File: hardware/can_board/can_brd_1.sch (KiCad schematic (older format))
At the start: 9 parts, among them P1 CONN_4, P2 CONN_2, U1 MCP2551

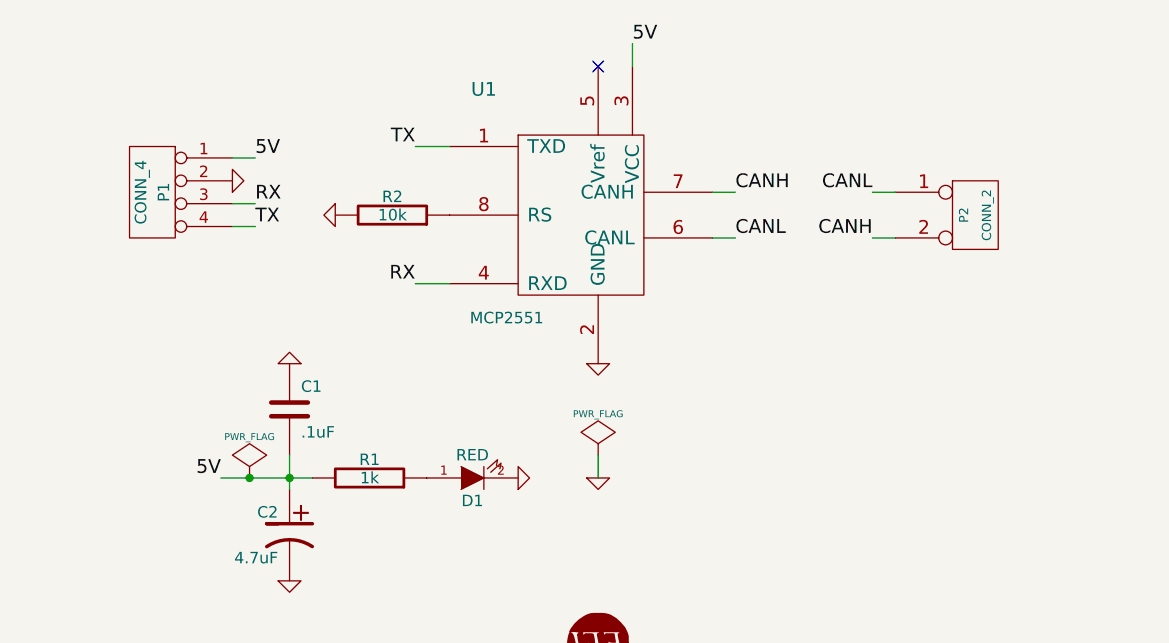
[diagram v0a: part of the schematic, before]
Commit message: 
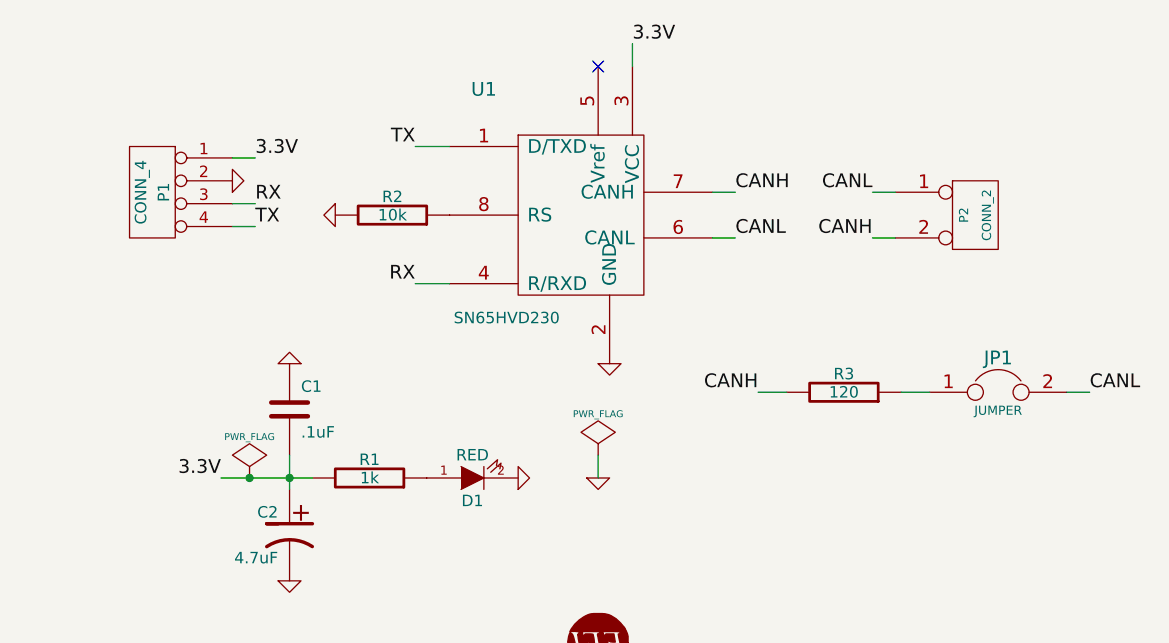
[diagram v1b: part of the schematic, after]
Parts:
- removed U1: MCP2551, symbol MCP2551
- added JP1: JUMPER, symbol JUMPER
- added R3: 120, symbol R
- added U1: SN65HVD230, symbol SN65HVD230
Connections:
- net CANH: now also R3.2, U1.7 (CANH)
- net CANL: now also JP1.2, U1.6 (CANL)
- net GND: now also U1.2 (GND)
- net RX: now also U1.4 (R/RXD)
- net TX: now also U1.1 (D/TXD)
- net at R2.1: now also U1.8 (RS)
- net 5V renamed 3.3V
- net 3.3V: now also U1.3 (VCC)
- new net: JP1.1, R3.1
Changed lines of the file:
@@
 Sheet 1 1
 Title ""
-Date "06 Янв 2014"
+Date "08 Янв 2014"
 Rev ""
 Comp ""
@@
 $EndComp
 Text Label 3250 3000 2    60   ~ 0
-5V
+3.3V
 $Comp
 L LOGO G1
@@
 $EndComp
 $Comp
-L MCP2551 U1
-U 1 1 52CADB33
-P 4800 1850
-F 0 "U1" H 4400 2400 60  0000 C CNN
-F 1 "MCP2551" H 4500 1400 50  0000 C CNN
-F 2 "" H 4800 1850 60  0000 C CNN
-F 3 "" H 4800 1850 60  0000 C CNN
-	1    4800 1850
-	1    0    0    -1
-$EndComp
-$Comp
 L GND #PWR05
 U 1 1 52CADB40
-P 4900 2500
-F 0 "#PWR05" H 4900 2500 30  0001 C CNN
-F 1 "GND" H 4900 2430 30  0001 C CNN
-F 2 "" H 4900 2500 60  0001 C CNN
-F 3 "" H 4900 2500 60  0001 C CNN
-	1    4900 2500
+P 4950 2500
+F 0 "#PWR05" H 4950 2500 30  0001 C CNN
+F 1 "GND" H 4950 2430 30  0001 C CNN
+F 2 "" H 4950 2500 60  0001 C CNN
+F 3 "" H 4950 2500 60  0001 C CNN
+	1    4950 2500
 	1    0    0    -1
 $EndComp
@@
 $EndComp
 Text Label 3400 1600 0    60   ~ 0
-5V
+3.3V
 $Comp
 L GND #PWR07
@@
 	5400 1950 5500 1950
 Text Label 5050 1100 0    60   ~ 0
-5V
+3.3V
 Wire Wire Line
 	5050 1200 5050 1100
@@
 	1    0    0    -1
 $EndComp
+$Comp
+L SN65HVD230 U1
+U 1 1 52CD2CA4
+P 4800 1850
+F 0 "U1" H 4400 2400 60  0000 C CNN
+F 1 "SN65HVD230" H 4500 1400 50  0000 C CNN
+F 2 "" H 4800 1850 60  0000 C CNN
+F 3 "" H 4800 1850 60  0000 C CNN
+	1    4800 1850
+	1    0    0    -1
+$EndComp
+$Comp
+L R R3
+U 1 1 52CD2DE2
+P 5975 2625
+F 0 "R3" V 6055 2625 50  0000 C CNN
+F 1 "120" V 5975 2625 50  0000 C CNN
+F 2 "" H 5975 2625 60  0001 C CNN
+F 3 "" H 5975 2625 60  0001 C CNN
+	1    5975 2625
+	0    1    -1   0
+$EndComp
+$Comp
+L JUMPER JP1
+U 1 1 52CD2DEF
+P 6650 2625
+F 0 "JP1" H 6650 2775 60  0000 C CNN
+F 1 "JUMPER" H 6650 2545 40  0000 C CNN
+F 2 "" H 6650 2625 60  0000 C CNN
+F 3 "" H 6650 2625 60  0000 C CNN
+	1    6650 2625
+	1    0    0    -1
+$EndComp
+Wire Wire Line
+	6225 2625 6350 2625
+Text Label 5600 2625 2    60   ~ 0
+CANH
+Text Label 7050 2625 0    60   ~ 0
+CANL
+Wire Wire Line
+	6950 2625 7050 2625
+Wire Wire Line
+	5725 2625 5600 2625
 $EndSCHEMATC

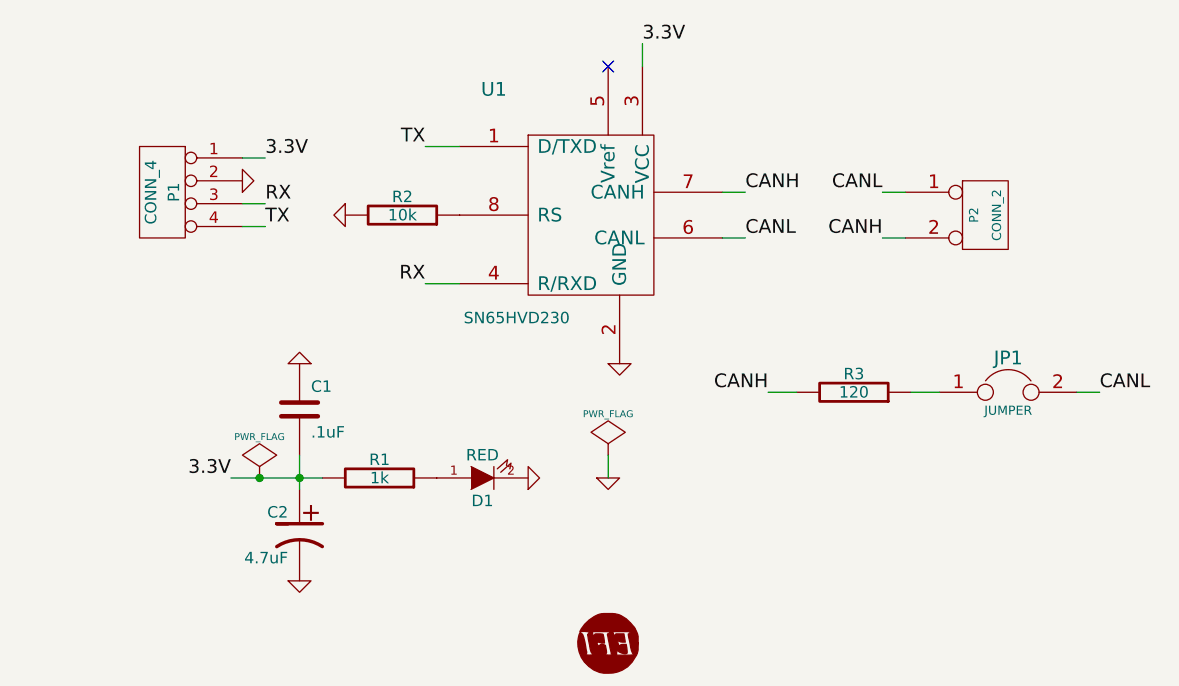
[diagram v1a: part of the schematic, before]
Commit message: 
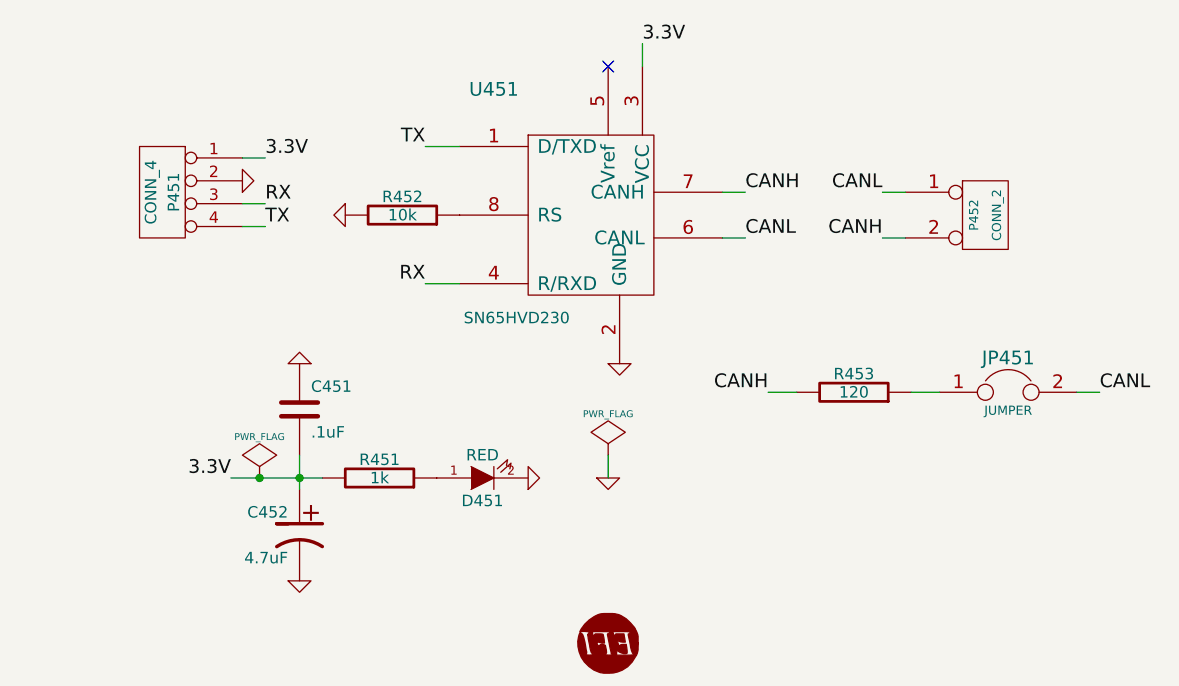
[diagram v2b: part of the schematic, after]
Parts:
- renumbered C1 to C451, C2 to C452, D1 to D451, G1 to G451, JP1 to JP451, P1 to P451, P2 to P452, R1 to R451, R2 to R452, R3 to R453, U1 to U451
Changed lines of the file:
@@
 $EndDescr
 $Comp
-L R R1
+L R R451
 U 1 1 52CAD8DB
 P 3900 3000
-F 0 "R1" V 3980 3000 50  0000 C CNN
+F 0 "R451" V 3980 3000 50  0000 C CNN
 F 1 "1k" V 3900 3000 50  0000 C CNN
 F 2 "" H 3900 3000 60  0001 C CNN
@@
 $EndComp
 $Comp
-L LED D1
+L LED D451
 U 1 1 52CAD8DC
 P 4350 3000
-F 0 "D1" H 4350 3100 50  0000 C CNN
+F 0 "D451" H 4350 3100 50  0000 C CNN
 F 1 "RED" H 4350 2900 50  0000 C CNN
 F 2 "" H 4350 3000 60  0001 C CNN
@@
 $EndComp
 $Comp
-L CP1 C2
+L CP1 C452
 U 1 1 52CAD8F6
 P 3550 3250
-F 0 "C2" H 3600 3350 50  0000 L CNN
+F 0 "C452" H 3600 3350 50  0000 L CNN
 F 1 "4.7uF" H 3600 3150 50  0000 L CNN
 F 2 "" H 3550 3250 60  0001 C CNN
@@
 $EndComp
 $Comp
-L C C1
+L C C451
 U 1 1 52CAD8F7
 P 3550 2700
-F 0 "C1" H 3600 2800 50  0000 L CNN
+F 0 "C451" H 3600 2800 50  0000 L CNN
 F 1 ".1uF" H 3600 2600 50  0000 L CNN
 F 2 "" H 3550 2700 60  0001 C CNN
@@
 3.3V
 $Comp
-L LOGO G1
+L LOGO G451
 U 1 1 52CADA22
 P 4900 3725
-F 0 "G1" H 4900 3622 60  0001 C CNN
+F 0 "G451" H 4900 3622 60  0001 C CNN
 F 1 "LOGO" H 4900 3828 60  0001 C CNN
 F 2 "" H 4900 3725 60  0000 C CNN
@@
 NoConn ~ 4900 1200
 $Comp
-L R R2
+L R R452
 U 1 1 52CADB46
 P 4000 1850
-F 0 "R2" V 4080 1850 50  0000 C CNN
+F 0 "R452" V 4080 1850 50  0000 C CNN
 F 1 "10k" V 4000 1850 50  0000 C CNN
 F 2 "" H 4000 1850 60  0001 C CNN
@@
 $EndComp
 $Comp
-L CONN_2 P2
+L CONN_2 P452
 U 1 1 52CADBC1
 P 6550 1850
-F 0 "P2" V 6500 1850 40  0000 C CNN
+F 0 "P452" V 6500 1850 40  0000 C CNN
 F 1 "CONN_2" V 6600 1850 40  0000 C CNN
 F 2 "" H 6550 1850 60  0000 C CNN
@@
 $EndComp
 $Comp
-L CONN_4 P1
+L CONN_4 P451
 U 1 1 52CADBD0
 P 2950 1750
-F 0 "P1" V 2900 1750 50  0000 C CNN
+F 0 "P451" V 2900 1750 50  0000 C CNN
 F 1 "CONN_4" V 3000 1750 50  0000 C CNN
 F 2 "" H 2950 1750 60  0000 C CNN
@@
 $EndComp
 $Comp
-L SN65HVD230 U1
+L SN65HVD230 U451
 U 1 1 52CD2CA4
 P 4800 1850
-F 0 "U1" H 4400 2400 60  0000 C CNN
+F 0 "U451" H 4400 2400 60  0000 C CNN
 F 1 "SN65HVD230" H 4500 1400 50  0000 C CNN
 F 2 "" H 4800 1850 60  0000 C CNN
@@
 $EndComp
 $Comp
-L R R3
+L R R453
 U 1 1 52CD2DE2
 P 5975 2625
-F 0 "R3" V 6055 2625 50  0000 C CNN
+F 0 "R453" V 6055 2625 50  0000 C CNN
 F 1 "120" V 5975 2625 50  0000 C CNN
 F 2 "" H 5975 2625 60  0001 C CNN
@@
 $EndComp
 $Comp
-L JUMPER JP1
+L JUMPER JP451
 U 1 1 52CD2DEF
 P 6650 2625
-F 0 "JP1" H 6650 2775 60  0000 C CNN
+F 0 "JP451" H 6650 2775 60  0000 C CNN
 F 1 "JUMPER" H 6650 2545 40  0000 C CNN
 F 2 "" H 6650 2625 60  0000 C CNN

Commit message: new location
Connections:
- net RX renamed CAN_RX
- net TX renamed CAN_TX
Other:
- moved on the sheet: P451
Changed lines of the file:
@@
 LIBS:art-electro-ic
 LIBS:logo_flipped
-LIBS:can_brd_1-cache
-EELAYER 24 0
+EELAYER 27 0
 EELAYER END
 $Descr A4 11693 8268
@@
 Sheet 1 1
 Title ""
-Date "08 Янв 2014"
+Date "19 jan 2014"
 Rev ""
 Comp ""
@@
 L CONN_4 P451
 U 1 1 52CADBD0
-P 2950 1750
-F 0 "P451" V 2900 1750 50  0000 C CNN
-F 1 "CONN_4" V 3000 1750 50  0000 C CNN
-F 2 "" H 2950 1750 60  0000 C CNN
-F 3 "" H 2950 1750 60  0000 C CNN
-	1    2950 1750
+P 2200 1750
+F 0 "P451" V 2150 1750 50  0000 C CNN
+F 1 "CONN_4" V 2250 1750 50  0000 C CNN
+F 2 "" H 2200 1750 60  0000 C CNN
+F 3 "" H 2200 1750 60  0000 C CNN
+	1    2200 1750
 	-1   0    0    -1
 $EndComp
-Text Label 3400 1600 0    60   ~ 0
+Text Label 2650 1600 0    60   ~ 0
 3.3V
 $Comp
 L GND #PWR07
 U 1 1 52CADB3B
-P 3300 1700
-F 0 "#PWR07" H 3300 1700 30  0001 C CNN
-F 1 "GND" H 3300 1630 30  0001 C CNN
-F 2 "" H 3300 1700 60  0001 C CNN
-F 3 "" H 3300 1700 60  0001 C CNN
-	1    3300 1700
+P 2550 1700
+F 0 "#PWR07" H 2550 1700 30  0001 C CNN
+F 1 "GND" H 2550 1630 30  0001 C CNN
+F 2 "" H 2550 1700 60  0001 C CNN
+F 3 "" H 2550 1700 60  0001 C CNN
+	1    2550 1700
 	0    -1   -1   0
 $EndComp
-Text Label 3400 1800 0    60   ~ 0
-RX
-Text Label 3400 1900 0    60   ~ 0
-TX
+Text Label 2650 1800 0    60   ~ 0
+CAN_RX
+Text Label 2650 1900 0    60   ~ 0
+CAN_TX
 Text Label 4100 1550 2    60   ~ 0
-TX
+CAN_TX
 Text Label 4100 2150 2    60   ~ 0
-RX
+CAN_RX
 Connection ~ -4675 3450
 Wire Wire Line
@@
 Connection ~ 3375 3000
 Wire Wire Line
-	3300 1800 3400 1800
-Wire Wire Line
-	3300 1900 3400 1900
-Wire Wire Line
-	3300 1600 3400 1600
+	2550 1800 2650 1800
+Wire Wire Line
+	2550 1900 2650 1900
+Wire Wire Line
+	2550 1600 2650 1600
 Wire Wire Line
 	4250 2150 4100 2150

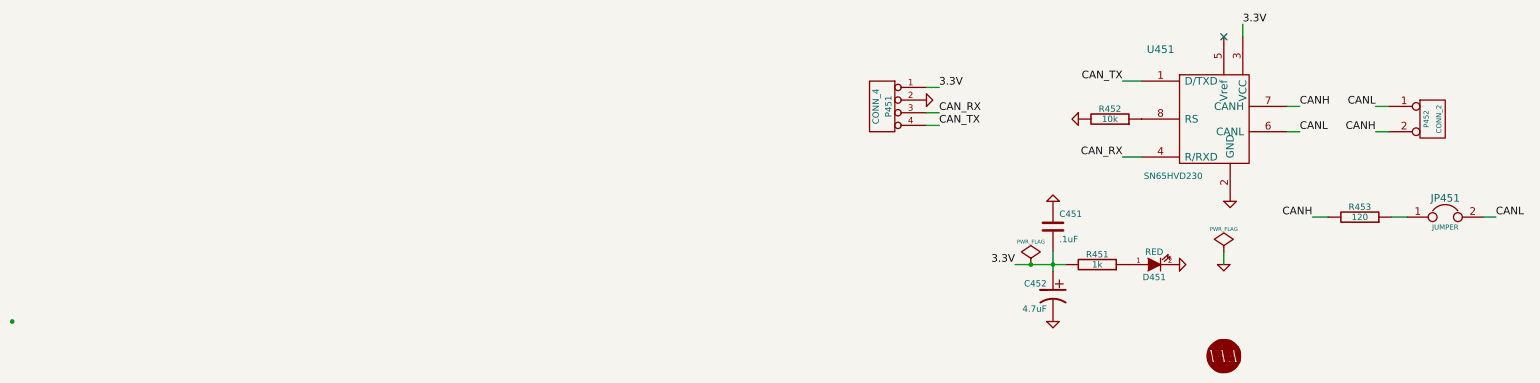
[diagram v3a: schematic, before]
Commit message: name range fix
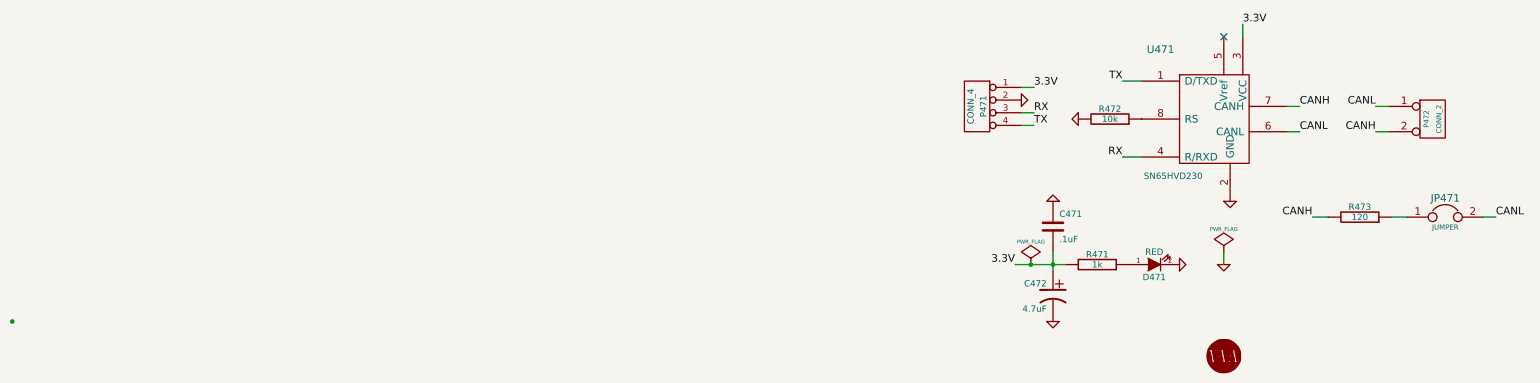
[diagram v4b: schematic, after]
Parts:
- renumbered C451 to C471, C452 to C472, D451 to D471, G451 to G471, JP451 to JP471, P451 to P471, P452 to P472, R451 to R471, R452 to R472, R453 to R473, U451 to U471
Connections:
- net CAN_RX renamed RX
- net CAN_TX renamed TX
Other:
- moved on the sheet: P471
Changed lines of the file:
@@
 LIBS:art-electro-ic
 LIBS:logo_flipped
-EELAYER 27 0
+LIBS:can_brd_1-cache
+EELAYER 24 0
 EELAYER END
 $Descr A4 11693 8268
@@
 Sheet 1 1
 Title ""
-Date "19 jan 2014"
+Date "08 Янв 2014"
 Rev ""
 Comp ""
@@
 $EndDescr
 $Comp
-L R R451
+L R R471
 U 1 1 52CAD8DB
 P 3900 3000
-F 0 "R451" V 3980 3000 50  0000 C CNN
+F 0 "R471" V 3980 3000 50  0000 C CNN
 F 1 "1k" V 3900 3000 50  0000 C CNN
 F 2 "" H 3900 3000 60  0001 C CNN
@@
 $EndComp
 $Comp
-L LED D451
+L LED D471
 U 1 1 52CAD8DC
 P 4350 3000
-F 0 "D451" H 4350 3100 50  0000 C CNN
+F 0 "D471" H 4350 3100 50  0000 C CNN
 F 1 "RED" H 4350 2900 50  0000 C CNN
 F 2 "" H 4350 3000 60  0001 C CNN
@@
 $EndComp
 $Comp
-L CP1 C452
+L CP1 C472
 U 1 1 52CAD8F6
 P 3550 3250
-F 0 "C452" H 3600 3350 50  0000 L CNN
+F 0 "C472" H 3600 3350 50  0000 L CNN
 F 1 "4.7uF" H 3600 3150 50  0000 L CNN
 F 2 "" H 3550 3250 60  0001 C CNN
@@
 $EndComp
 $Comp
-L C C451
+L C C471
 U 1 1 52CAD8F7
 P 3550 2700
-F 0 "C451" H 3600 2800 50  0000 L CNN
+F 0 "C471" H 3600 2800 50  0000 L CNN
 F 1 ".1uF" H 3600 2600 50  0000 L CNN
 F 2 "" H 3550 2700 60  0001 C CNN
@@
 3.3V
 $Comp
-L LOGO G451
+L LOGO G471
 U 1 1 52CADA22
 P 4900 3725
-F 0 "G451" H 4900 3622 60  0001 C CNN
+F 0 "G471" H 4900 3622 60  0001 C CNN
 F 1 "LOGO" H 4900 3828 60  0001 C CNN
 F 2 "" H 4900 3725 60  0000 C CNN
@@
 NoConn ~ 4900 1200
 $Comp
-L R R452
+L R R472
 U 1 1 52CADB46
 P 4000 1850
-F 0 "R452" V 4080 1850 50  0000 C CNN
+F 0 "R472" V 4080 1850 50  0000 C CNN
 F 1 "10k" V 4000 1850 50  0000 C CNN
 F 2 "" H 4000 1850 60  0001 C CNN
@@
 $EndComp
 $Comp
-L CONN_2 P452
+L CONN_2 P472
 U 1 1 52CADBC1
 P 6550 1850
-F 0 "P452" V 6500 1850 40  0000 C CNN
+F 0 "P472" V 6500 1850 40  0000 C CNN
 F 1 "CONN_2" V 6600 1850 40  0000 C CNN
 F 2 "" H 6550 1850 60  0000 C CNN
@@
 $EndComp
 $Comp
-L CONN_4 P451
+L CONN_4 P471
 U 1 1 52CADBD0
-P 2200 1750
-F 0 "P451" V 2150 1750 50  0000 C CNN
-F 1 "CONN_4" V 2250 1750 50  0000 C CNN
-F 2 "" H 2200 1750 60  0000 C CNN
-F 3 "" H 2200 1750 60  0000 C CNN
-	1    2200 1750
+P 2950 1750
+F 0 "P471" V 2900 1750 50  0000 C CNN
+F 1 "CONN_4" V 3000 1750 50  0000 C CNN
+F 2 "" H 2950 1750 60  0000 C CNN
+F 3 "" H 2950 1750 60  0000 C CNN
+	1    2950 1750
 	-1   0    0    -1
 $EndComp
-Text Label 2650 1600 0    60   ~ 0
+Text Label 3400 1600 0    60   ~ 0
 3.3V
 $Comp
 L GND #PWR07
 U 1 1 52CADB3B
-P 2550 1700
-F 0 "#PWR07" H 2550 1700 30  0001 C CNN
-F 1 "GND" H 2550 1630 30  0001 C CNN
-F 2 "" H 2550 1700 60  0001 C CNN
-F 3 "" H 2550 1700 60  0001 C CNN
-	1    2550 1700
+P 3300 1700
+F 0 "#PWR07" H 3300 1700 30  0001 C CNN
+F 1 "GND" H 3300 1630 30  0001 C CNN
+F 2 "" H 3300 1700 60  0001 C CNN
+F 3 "" H 3300 1700 60  0001 C CNN
+	1    3300 1700
 	0    -1   -1   0
 $EndComp
-Text Label 2650 1800 0    60   ~ 0
-CAN_RX
-Text Label 2650 1900 0    60   ~ 0
-CAN_TX
+Text Label 3400 1800 0    60   ~ 0
+RX
+Text Label 3400 1900 0    60   ~ 0
+TX
 Text Label 4100 1550 2    60   ~ 0
-CAN_TX
+TX
 Text Label 4100 2150 2    60   ~ 0
-CAN_RX
+RX
 Connection ~ -4675 3450
 Wire Wire Line
@@
 Connection ~ 3375 3000
 Wire Wire Line
-	2550 1800 2650 1800
-Wire Wire Line
-	2550 1900 2650 1900
-Wire Wire Line
-	2550 1600 2650 1600
+	3300 1800 3400 1800
+Wire Wire Line
+	3300 1900 3400 1900
+Wire Wire Line
+	3300 1600 3400 1600
 Wire Wire Line
 	4250 2150 4100 2150
@@
 $EndComp
 $Comp
-L SN65HVD230 U451
+L SN65HVD230 U471
 U 1 1 52CD2CA4
 P 4800 1850
-F 0 "U451" H 4400 2400 60  0000 C CNN
+F 0 "U471" H 4400 2400 60  0000 C CNN
 F 1 "SN65HVD230" H 4500 1400 50  0000 C CNN
 F 2 "" H 4800 1850 60  0000 C CNN
@@
 $EndComp
 $Comp
-L R R453
+L R R473
 U 1 1 52CD2DE2
 P 5975 2625
-F 0 "R453" V 6055 2625 50  0000 C CNN
+F 0 "R473" V 6055 2625 50  0000 C CNN
 F 1 "120" V 5975 2625 50  0000 C CNN
 F 2 "" H 5975 2625 60  0001 C CNN
@@
 $EndComp
 $Comp
-L JUMPER JP451
+L JUMPER JP471
 U 1 1 52CD2DEF
 P 6650 2625
-F 0 "JP451" H 6650 2775 60  0000 C CNN
+F 0 "JP471" H 6650 2775 60  0000 C CNN
 F 1 "JUMPER" H 6650 2545 40  0000 C CNN
 F 2 "" H 6650 2625 60  0000 C CNN
